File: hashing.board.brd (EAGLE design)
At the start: 160 x 100 mm, 144 parts, among them U1 ASIC-1, U10 EPM570GT100C5N, U2 ASIC-1, U3 ASIC-1, U4 ASIC-1, U5 ASIC-1, U6 ASIC-1, U7 ASIC-1, U8 ASIC-1, U9 AT32UC3A1256-AUT, X1 5566-8, X2 5566-8, X3 MINI-USB-32005-301, X4 22-23-2031

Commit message: After the new crazy caps
before the placement and routing though
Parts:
- moved CA2 130.1 mm to (44.8, 16.7), flipped to the bottom
- moved CA1 12.4 mm to (25.0, 25.0), turned to 180 degrees
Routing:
- net VDD-1VA: track 162.5 -> 118.5 mm, vias 97 -> 74
- net GND: track 292.8 -> 285.8 mm

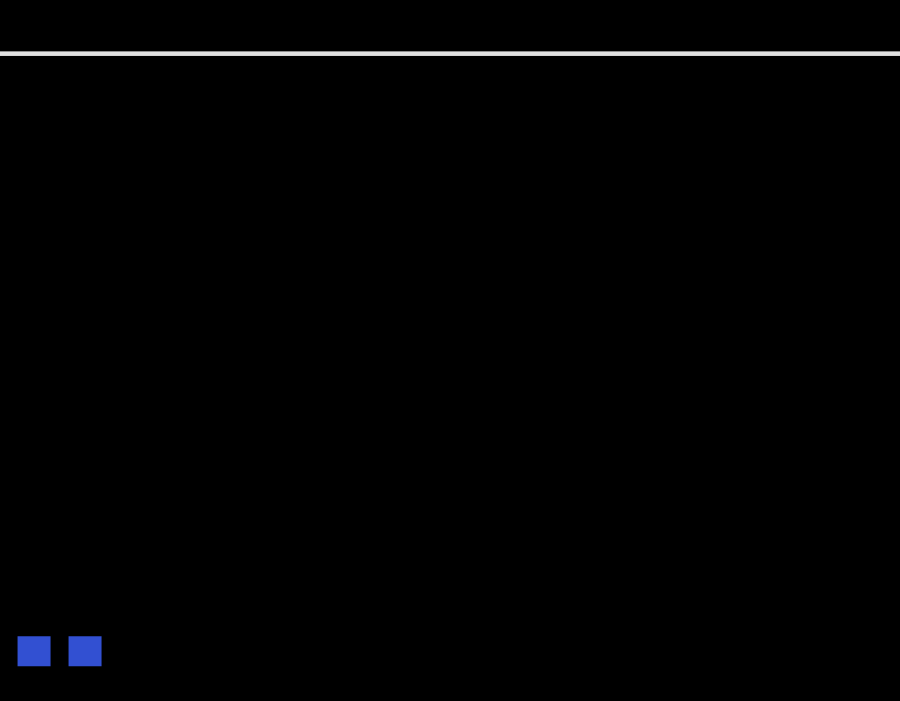
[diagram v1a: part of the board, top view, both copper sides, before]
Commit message: new custom bga pkg layout
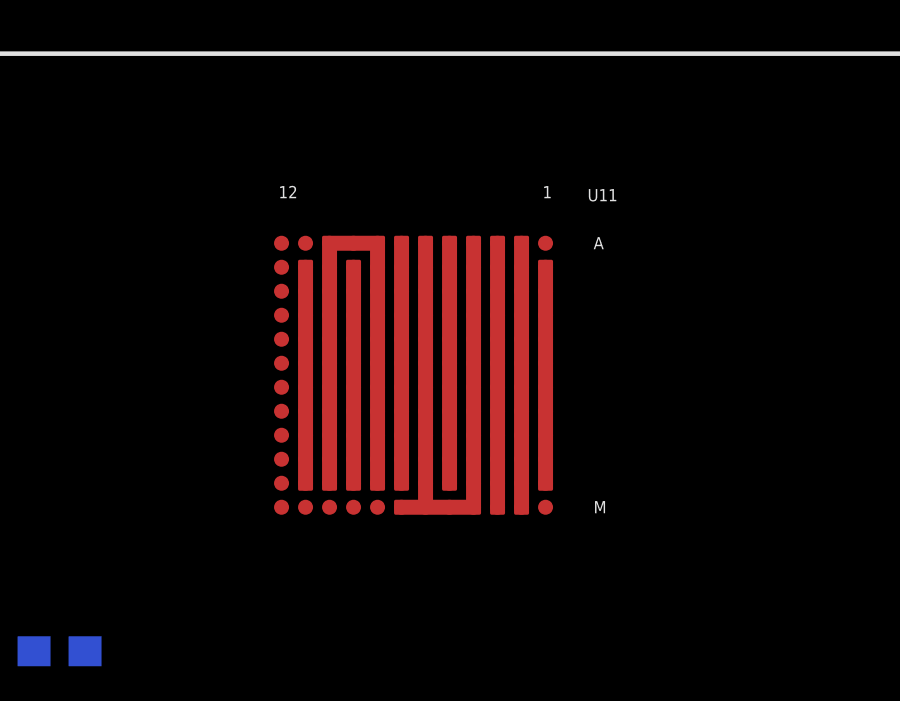
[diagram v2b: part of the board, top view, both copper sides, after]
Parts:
- added U11: BFL-ASIC-1, BFL.new:BFL-BGA-BIG-PADS
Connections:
- new net VDD: U11.A10, U11.A2, U11.A4, U11.A6, U11.A8, U11.A9, U11.B10, U11.B2, U11.B4, U11.B6, U11.B8, U11.C10, U11.C2, U11.C4, U11.C6, U11.C8, U11.D10, U11.D2, U11.D4, U11.D6, U11.D8, U11.E10, U11.E2, U11.E4, U11.E6, U11.E8, U11.F10, U11.F2, U11.F4, U11.F6, U11.F8, U11.G10, U11.G2, U11.G4, U11.G6, U11.G8, U11.H10, U11.H2, U11.H4, U11.H6, U11.H8, U11.J10, U11.J2, U11.J4, U11.J6, U11.J8, U11.K10, U11.K2, U11.K4, U11.K6, U11.K8, U11.L10, U11.L2, U11.L4, U11.L6, U11.L8, U11.M2, U11.M4, U11.M5, U11.M6, U11.M7
- new net VDD-IO-3V3: U11.A11, U11.M10
- net GND: now also U11.A3, U11.A5, U11.A7, U11.B1, U11.B11, U11.B3, U11.B5, U11.B7, U11.B9, U11.C1, U11.C11, U11.C3, U11.C5, U11.C7, U11.C9, U11.D1, U11.D11, U11.D3, U11.D5, U11.D7, U11.D9, U11.E1, U11.E11, U11.E3, U11.E5, U11.E7, U11.E9, U11.F1, U11.F11, U11.F3, U11.F5, U11.F7, U11.F9, U11.G1, U11.G11, U11.G3, U11.G5, U11.G7, U11.G9, U11.H1, U11.H11, U11.H3, U11.H5, U11.H7, U11.H9, U11.J1, U11.J11, U11.J3, U11.J5, U11.J7, U11.J9, U11.K1, U11.K11, U11.K3, U11.K5, U11.K7, U11.K9, U11.L1, U11.L11, U11.L3, U11.L5, U11.L7, U11.L9, U11.M3

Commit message: broken
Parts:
- moved CA2 45.4 mm to (49.2, 61.9)
